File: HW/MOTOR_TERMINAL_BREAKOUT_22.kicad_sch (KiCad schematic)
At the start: 11 parts

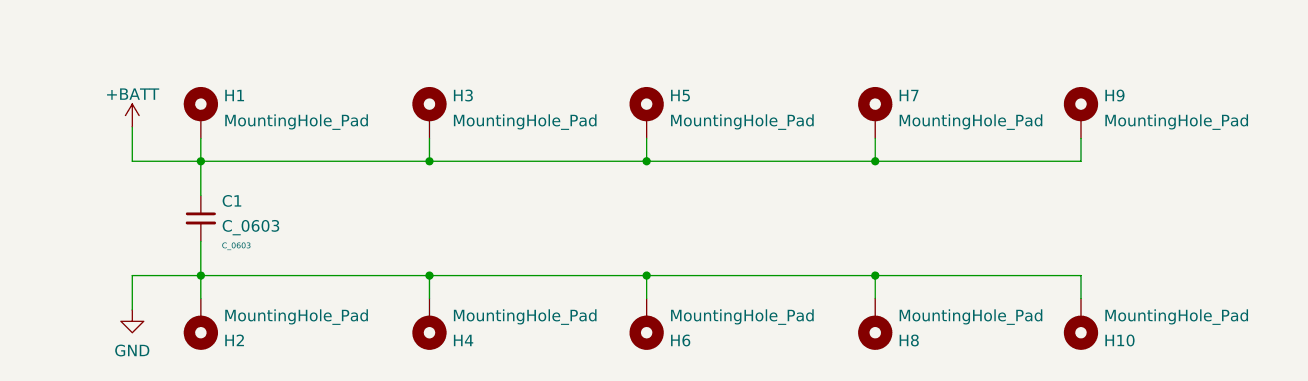
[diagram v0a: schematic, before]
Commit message: Update design to v1.1 for next manufacturing run
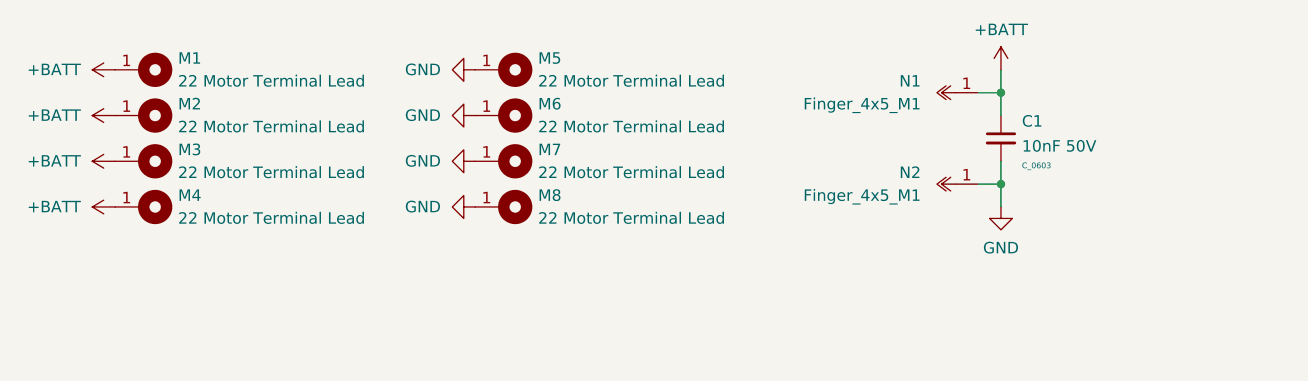
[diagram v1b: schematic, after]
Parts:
- removed H1, H2: MountingHole_Pad, MountingHole:MountingHole_3.2mm_M3_ISO7380_Pad_TopBottom, symbol Mechanical:MountingHole_Pad
- removed H10, H3, H4, H5, H6, H7, H8, H9: MountingHole_Pad, MountingHole:MountingHole_3mm_Pad_TopBottom, symbol Mechanical:MountingHole_Pad
- added M1, M2, M3, M4, M5, M6, M7, M8: 22 Motor Terminal Lead, MOTOR_TERMINAL_BREAKOUT:22 Motor Terminal Lead, symbol MOTOR_TERMINAL_BREAKOUT:22 Motor Terminal Lead
- added N1, N2: Finger_4x5_M1, N_NonPart:Finger_4x5_M1, symbol N_NonPart:Finger_4x5_M1
- C1: value C_0603 -> 10nF 50V; LCSC_Part (none) -> C100042; MFG Part (none) -> CC0603KRX7R9BB103
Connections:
- net +BATT: now also M1.1, M2.1, M3.1, M4.1, N1.1
- net GND: now also M5.1, M6.1, M7.1, M8.1, N2.1
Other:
- title: N20 FACEPLATE -> MOTOR TERMINAL BREAKOUT 22mm
- moved on the sheet: C1
